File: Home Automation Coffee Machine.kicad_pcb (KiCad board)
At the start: 2 copper layers, 46.4 x 46.4 mm, 49 parts, among them J1 Conn_01x08_Male

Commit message: revision 2.3
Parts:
- removed ESP32-WROOM32: ESP32-WROOM-32, RF_Module:ESP32-WROOM-32
- removed PC3: 2.2uF, Capacitor_SMD:C_1206_3216Metric
- added BZ1: Buzzer, Buzzer_Beeper:MagneticBuzzer_Kobitone_254-EMB84Q-RO, B.Cu at (152.6, 107.7)
- added ESP32-S3-WROOM1: ESP32-S3-WROOM1, RF_Module:ESP32-WROOM-32, F.Cu at (151.9, 95.7)
- added WaterLevel1: WaterLevel, Connector_JST:JST_EH_B2B-EH-A_1x02_P2.50mm_Vertical, B.Cu at (130.0, 112.3)
- ExtSW1: footprint TerminalBlock_4Ucon:TerminalBlock_4Ucon_1x03_P3.50mm_Horizontal -> TerminalBlock_4Ucon:TerminalBlock_4Ucon_1x03_P3.50mm_Vertical
- moved G*** 14.3 mm to (160.8, 99.6), turned to -90 degrees
- moved NEXTIONLCD1 4.49 mm to (144.1, 112.6)
- moved ExtSW1 1.13 mm to (123.3, 107.7)
- moved G*** 0.83 mm to (133.0, 79.4)
- moved G*** 0.59 mm to (141.2, 98.1)
- moved PWR220 0.33 mm to (138.2, 74.0)
- moved TEMPMX1 0.28 mm to (123.3, 86.4)
- moved ExtPW1 0.22 mm to (123.3, 95.3)
- moved PWR5V0 0.17 mm to (151.4, 75.2)
- moved ENR1 0.07 mm to (148.8, 106.9)
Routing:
- net /IO24_WaterLevel: track 0.00 -> 63.3 mm, vias 0 -> 1
- net /IO3RX: track 21.7 -> 0.00 mm, vias 1 -> 0
- net /IO03RX: track 0.00 -> 21.7 mm, vias 0 -> 1
- net /IO19_BUZ: track 0.00 -> 21.6 mm, vias 0 -> 1
- net /GND: track 209.4 -> 215.8 mm, vias 14 -> 13
- net /5V0: track 57.9 -> 60.0 mm, vias 4 -> 5
- net /RST_EN_RTS: track 20.1 -> 22.2 mm, vias 1 -> 3
- net /IO16_U2RX_nexTx: track 40.9 -> 42.4 mm
- net /IO12_grinder: track 52.1 -> 51.0 mm
- net /IO01TX: track 22.7 -> 21.6 mm
- net /TX_IN: track 19.9 -> 20.9 mm
- net /RX_IN: track 25.2 -> 26.0 mm
- net /IO17_U2TX_nexRx: track 43.7 -> 42.9 mm
- net /IO04_H2O: track 44.9 -> 44.2 mm
- net /3V3: track 142.0 -> 142.6 mm
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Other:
- board text added: "C"
- board text added: "Copyright 2022 rev. 2.3"
- board text added: "D"
- board text added: "G"
- board text added: "W"
- board text added: "Water Level"
- board text removed: "Coffee"
- board text removed: "Copyright 2022 rev. 2.0"
- board text removed: "Grinder"
- board text removed: "Water"

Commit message: rev. 2.4
improved  relay connectivity. New 3.3V power converter.
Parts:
- removed HX4002B1: PWIC, AeonLabs:HX4002 SOT95 P280X125-6N
- removed HX4002B2: PWIC1, AeonLabs:HX4002 SOT95 P280X125-6N
- removed PC1, PC2, PC4: 2.2uF, Capacitor_SMD:C_1206_3216Metric
- added Coffee1: QD2, TestPoint:TestPoint_Pad_Bridge_1.0x1.0mm, B.Cu at (124.3, 103.3)
- added Grinder1: QD3, TestPoint:TestPoint_Pad_Bridge_1.0x1.0mm, B.Cu at (120.4, 109.4)
- added MC1: 28uF, Capacitor_SMD:C_0805_2012Metric_Pad1.18x1.45mm_HandSolder, F.Cu at (128.3, 103.2)
- added MC2: 28uF, Capacitor_SMD:C_0805_2012Metric_Pad1.18x1.45mm_HandSolder, F.Cu at (130.5, 109.7)
- added MD1: SS36, Diode_SMD:D_2010_5025Metric_Pad1.52x2.65mm_HandSolder, F.Cu at (132.1, 107.0)
- added ML1: ????, Inductor_SMD:L_0805_2012Metric_Pad1.15x1.40mm_HandSolder, F.Cu at (133.6, 102.1)
- added MR1: 2.2k, Resistor_SMD:R_0805_2012Metric_Pad1.20x1.40mm_HandSolder, F.Cu at (131.4, 98.5)
- added MR2: 5V=15K; 3.3v=10k, Resistor_SMD:R_0805_2012Metric_Pad1.20x1.40mm_HandSolder, F.Cu at (128.3, 99.4)
- added MT_VIN1: VIN, TestPoint:TestPoint_Pad_D1.5mm, F.Cu at (127.3, 107.9)
- added MT_VOUT1: VOUT, TestPoint:TestPoint_Pad_D1.5mm, F.Cu at (126.8, 110.1)
- added Q1: 2TY, Package_TO_SOT_SMD:SOT-23, F.Cu at (120.4, 98.8)
- added Q2: 2TY, Package_TO_SOT_SMD:SOT-23, F.Cu at (122.3, 108.8)
- added Q3: 2TY, Package_TO_SOT_SMD:SOT-23, F.Cu at (124.7, 104.3)
- added QR1: 4K7, Resistor_SMD:R_0805_2012Metric_Pad1.20x1.40mm_HandSolder, F.Cu at (123.7, 98.4)
- added QR2: 4K7, Resistor_SMD:R_0805_2012Metric_Pad1.20x1.40mm_HandSolder, F.Cu at (119.4, 108.8)
- added QR3: 4K7, Resistor_SMD:R_0805_2012Metric_Pad1.20x1.40mm_HandSolder, F.Cu at (124.7, 101.6)
- added U1: MT3608, Converter_DCDC:MT3608 SOT95P280X145-6N, F.Cu at (130.9, 102.0)
- added h20: QD1, TestPoint:TestPoint_Pad_Bridge_1.0x1.0mm, B.Cu at (122.8, 98.7)
- ExtPW1: footprint TerminalBlock_4Ucon:TerminalBlock_4Ucon_1x02_P3.50mm_Vertical -> Connector_JST:JST_PH_B2B-PH-K_1x02_P2.00mm_Vertical
- ExtSW1: footprint TerminalBlock_4Ucon:TerminalBlock_4Ucon_1x03_P3.50mm_Vertical -> Connector_JST:JST_PH_B3B-PH-K_1x03_P2.00mm_Vertical
- moved H3 17.1 mm to (83.1, 112.0)
- moved H2 15.3 mm to (90.2, 112.1)
- moved G*** 10.1 mm to (86.7, 79.2)
- moved H1 7.41 mm to (82.4, 106.7)
- moved H4 7.41 mm to (89.6, 106.7)
- moved ExtSW1 2.42 mm to (121.5, 106.0)
- moved ExtPW1 1.72 mm to (121.6, 95.2)
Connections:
- net /3V3 renamed 3V3
- BZ1 pad 2: /GND -> GND
- CJ11 pad 1: /GND -> GND
- ESP32-S3-WROOM1 pad 1: /GND -> GND
- ESP32-S3-WROOM1 pad 14: /IO12_grinder -> /IO12_Coffee
- ESP32-S3-WROOM1 pad 15: /GND -> GND
- ESP32-S3-WROOM1 pad 23: /IO15_Coffee -> /IO15_grinder
- ESP32-S3-WROOM1 pad 38: /GND -> GND
- ESP32-S3-WROOM1 pad 39: /GND -> GND
- ESPC1 pad 2: /GND -> GND
- ESPC2 pad 2: /GND -> GND
- ESP_EN_C1 pad 1: /GND -> GND
- ExtPW1 pad 2: /GND -> GND
- ExtSW1 pad 1: /IO12_grinder -> Net-(ExtSW1-Pad1)
- ExtSW1 pad 2: /IO15_Coffee -> Net-(ExtSW1-Pad2)
- ExtSW1 pad 3: /IO04_H2O -> Net-(ExtSW1-Pad3)
- Fuse1 pad 1: /5V0 -> 5V0
- J1 pad 2: /GND -> GND
- LED1 pad 4: /GND -> GND
- MAX66751 pad 1: /GND -> GND
- MXC1 pad 1: /GND -> GND
- NEXTIONLCD1 pad 1: /5V0 -> 5V0
- NEXTIONLCD1 pad 4: /GND -> GND
- OUT1 pad 1: /GND -> GND
- PWR5V0 pad 1: /GND -> GND
- TEMPDS1 pad 3: /GND -> GND
- VL53L0X1 pad 2: /GND -> GND
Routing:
- net /GND: track 215.8 -> 0.00 mm, vias 13 -> 0
- net GND: track 0.00 -> 213.0 mm, vias 0 -> 13
- net 5V0: track 0.00 -> 67.3 mm, vias 0 -> 4
- net /5V0: track 60.0 -> 0.00 mm, vias 5 -> 0
- net /IO15_grinder: track 0.00 -> 58.4 mm, vias 0 -> 2
- net /IO12_grinder: track 51.0 -> 0.00 mm, vias 1 -> 0
- net /IO15_Coffee: track 46.7 -> 0.00 mm, vias 1 -> 0
- net /IO12_Coffee: track 0.00 -> 45.4 mm, vias 0 -> 1
- net /IO3RX: track 0.00 -> 21.7 mm, vias 0 -> 1
- net /IO03RX: track 21.7 -> 0.00 mm, vias 1 -> 0
- net 3V3: track 142.6 -> 158.5 mm, vias 9 -> 8
- net Net-(MD1-Pad2): track 0.00 -> 9.22 mm
- net Net-(ExtSW1-Pad2): track 0.00 -> 7.99 mm
- net Net-(ExtSW1-Pad3): track 0.00 -> 6.22 mm
- net Net-(ExtSW1-Pad1): track 0.00 -> 5.61 mm
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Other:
- board text added: "Copyright 2022 rev. 2.4"
- board text added: "DC2DC [1.8;28]V up/down"
- board text added: "V-IN"
- board text added: "V-OUT"
- board text removed: "Copyright 2022 rev. 2.3"

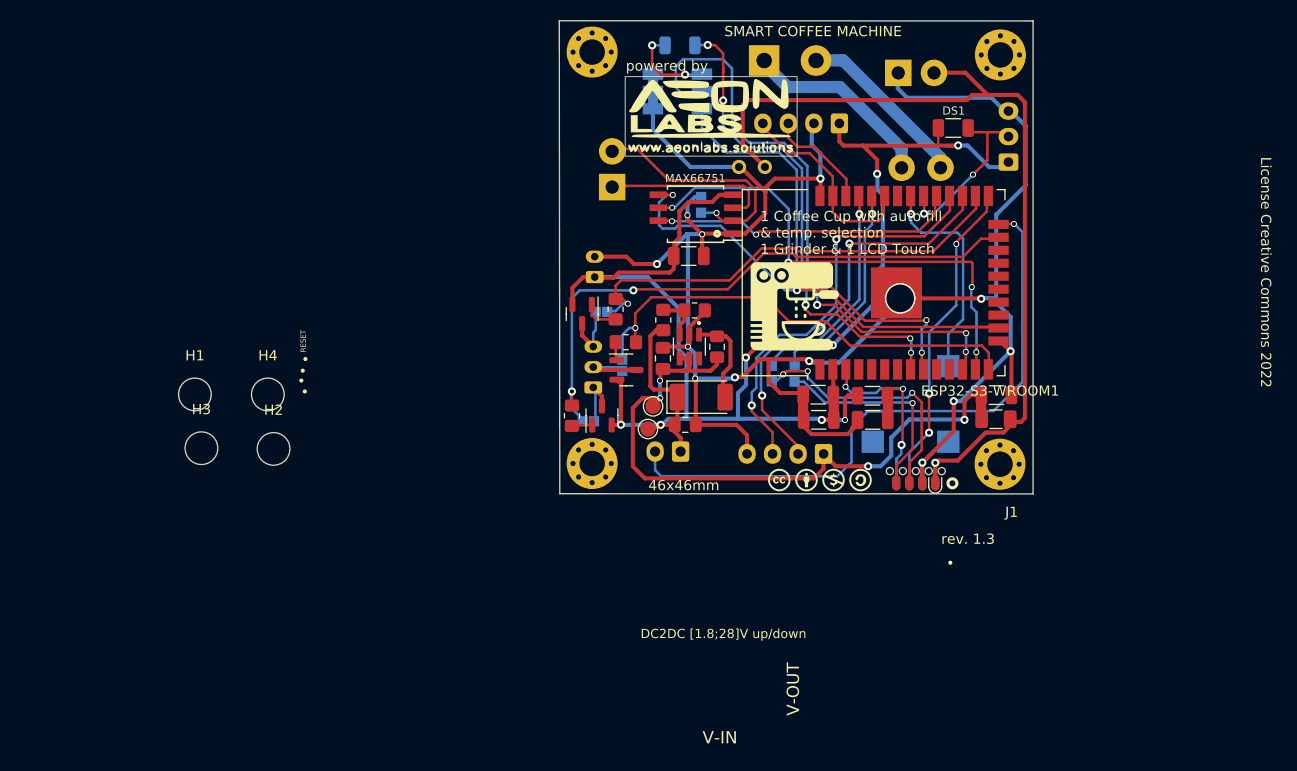
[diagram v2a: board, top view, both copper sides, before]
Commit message: rev. 2.5
correction to the power supply.
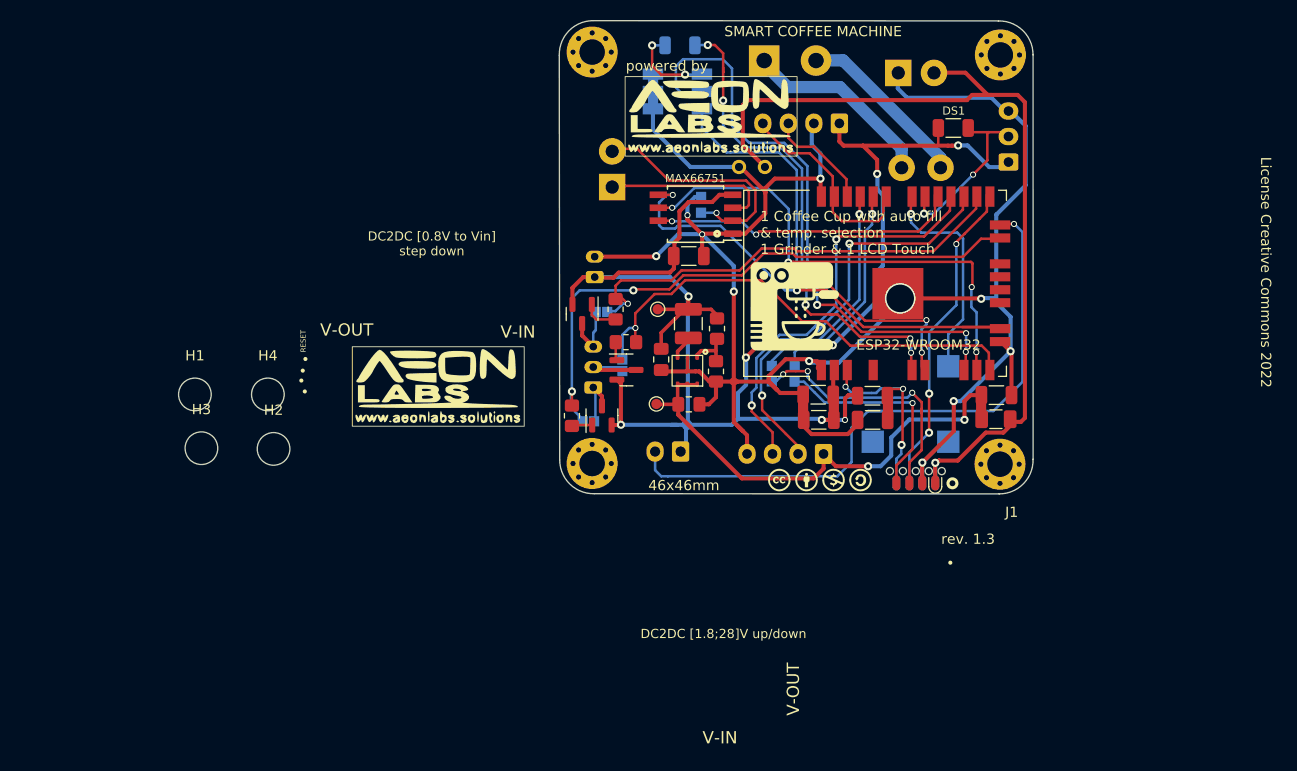
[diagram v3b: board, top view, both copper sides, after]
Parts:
- removed ESP32-S3-WROOM1: ESP32-S3-WROOM1, RF_Module:ESP32-WROOM-32
- removed MC1, MC2: 28uF, Capacitor_SMD:C_0805_2012Metric_Pad1.18x1.45mm_HandSolder
- removed MD1: SS36, Diode_SMD:D_2010_5025Metric_Pad1.52x2.65mm_HandSolder
- removed MR1: 2.2k, Resistor_SMD:R_0805_2012Metric_Pad1.20x1.40mm_HandSolder
- removed MR2: 5V=15K; 3.3v=10k, Resistor_SMD:R_0805_2012Metric_Pad1.20x1.40mm_HandSolder
- removed MT_VIN1: VIN, TestPoint:TestPoint_Pad_D1.5mm
- removed MT_VOUT1: VOUT, TestPoint:TestPoint_Pad_D1.5mm
- removed U1: MT3608, Converter_DCDC:MT3608 SOT95P280X145-6N
- added AC1: 22uF, Capacitor_SMD:C_0805_2012Metric_Pad1.18x1.45mm_HandSolder, F.Cu at (128.1, 103.3)
- added AC2: 4.7uF, Capacitor_SMD:C_0805_2012Metric_Pad1.18x1.45mm_HandSolder, F.Cu at (130.8, 107.7)
- added AR1: 3V3=1K5, Resistor_SMD:R_0805_2012Metric_Pad1.20x1.40mm_HandSolder, F.Cu at (133.6, 100.3)
- added AR2: 3V3=470R, Resistor_SMD:R_0805_2012Metric_Pad1.20x1.40mm_HandSolder, F.Cu at (133.5, 104.5)
- added AU1: AUR9718x_DFN_3x3mm_6_pin, Package_DFN_QFN:AUR9718 3x3mm 6 pin, F.Cu at (130.8, 104.5)
- added ESP32-WROOM32: ESP32-WROOM32, RF_Module:ESP32-WROOM-32, F.Cu at (152.1, 95.8)
- added G***: LOGO, AeonLabs Logosy:aeon logo www, F.Cu at (106.3, 105.9)
- added TP1: VIN, TestPoint:TestPoint_Pad_D1.0mm, F.Cu at (127.7, 107.7)
- added TP2: VOut, TestPoint:TestPoint_Pad_D1.0mm, F.Cu at (127.8, 98.4)
- ML1: value ???? -> 3.3uF; footprint Inductor_SMD:L_0805_2012Metric_Pad1.15x1.40mm_HandSolder -> Inductor_SMD:L_1210_3225Metric
- moved ML1 3.61 mm to (130.8, 99.8), turned to -90 degrees
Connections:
- ML1 pad 1: 5V0 -> 3V3
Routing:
- net /IO3RX: track 21.7 -> 0.00 mm, vias 1 -> 0
- net /IO03RX: track 0.00 -> 21.7 mm, vias 0 -> 1
- net 5V0: track 67.3 -> 49.9 mm, vias 4 -> 2
- net Net-(AU1-Pad3): track 9.22 -> 2.40 mm
- net Net-(MR1-Pad1): track 4.66 -> 0.00 mm
- net Net-(AR1-Pad2): track 0.00 -> 4.48 mm
- net /IO12_Coffee: track 45.4 -> 46.8 mm
- net 3V3: track 158.5 -> 157.5 mm
- net GND: track 213.0 -> 212.5 mm, vias 13 -> 11
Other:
- outline, holes or cut-outs redrawn
- board text added: "Copyright 2022 rev. 2.5"
- board text added: "DC2DC [0.8V to Vin] step down"
- board text removed: "Copyright 2022 rev. 2.4"
